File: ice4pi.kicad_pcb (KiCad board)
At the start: 4 copper layers, 85 x 56 mm, 40 parts, among them J1 Conn_02x03, J2 Raspberry_Pi_2_3, J3 USB_C_Receptacle_USB2.0, J4 RJ45_Abracon_ARJP11A-MASA-B-A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, U1 ENC28J60x-SS, U2 DSC1001DE1-025.0000, U3 TPS2375-1

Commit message: fix: better paths
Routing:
- net POE_V-: track 73.7 -> 71.0 mm
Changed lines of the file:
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@@
 	)
 	(via
-		(at 98.5 76.5)
+		(at 101 79)
 		(size 0.8)
 		(drill 0.4)
@@
 	)
 	(segment
-		(start 97 84)
-		(end 97 78)
+		(start 105.5 83.5)
+		(end 105.5 90)
 		(width 1)
 		(layer "In1.Cu")
@@
 	)
 	(segment
-		(start 97 78)
-		(end 98.5 76.5)
-		(width 1)
-		(layer "In1.Cu")
-		(net 50)
-	)
-	(segment
-		(start 105.5 90)
-		(end 103 90)
-		(width 1)
-		(layer "In1.Cu")
-		(net 50)
-	)
-	(segment
-		(start 103 90)
-		(end 97 84)
+		(start 101 79)
+		(end 105.5 83.5)
 		(width 1)
 		(layer "In1.Cu")
@@
 	)
 	(segment
+		(start 101 79)
+		(end 97.4 75.4)
+		(width 1)
+		(layer "B.Cu")
+		(net 50)
+	)
+	(segment
 		(start 107.5 97.5)
 		(end 106 97.5)
@@
 	)
 	(segment
-		(start 98.5 76.5)
-		(end 97.4 75.4)
+		(start 97.4 73.1)
+		(end 102.5 68)
 		(width 1)
 		(layer "B.Cu")
@@
 		(width 1)
 		(layer "B.Cu")
-		(net 50)
-	)
-	(segment
-		(start 97.4 73.1)
-		(end 102.5 68)
-		(width 1)
-		(layer "B.Cu")

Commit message: fix: led
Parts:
- added R12: 332K, Resistor_SMD:R_0402_1005Metric, F.Cu at (103.0, 101.2)
- moved R7 0.10 mm to (132.8, 71.5)
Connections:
- R6 pad 1: /LEDB -> /LEDA
- R6 pad 2: Net-(J4-Pad13) -> Net-(J4-Pad11)
- R7 pad 1: /LEDA -> /LEDB
- R7 pad 2: Net-(J4-Pad11) -> Net-(J4-Pad13)
- U3 pad 6: Net-(LSI-U1-S2) -> Net-(U3-PG)
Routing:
- net (no net): track 23.1 -> 0.00 mm
- net Net-(J4-Pad13): track 0.00 -> 17.3 mm
- net Net-(J4-Pad11): track 0.00 -> 5.77 mm
- net Net-(LSI-U1-S2): track 13.4 -> 11.6 mm
- net Net-(U3-PG): track 0.00 -> 1.62 mm
- net +5V: vias 3 -> 5

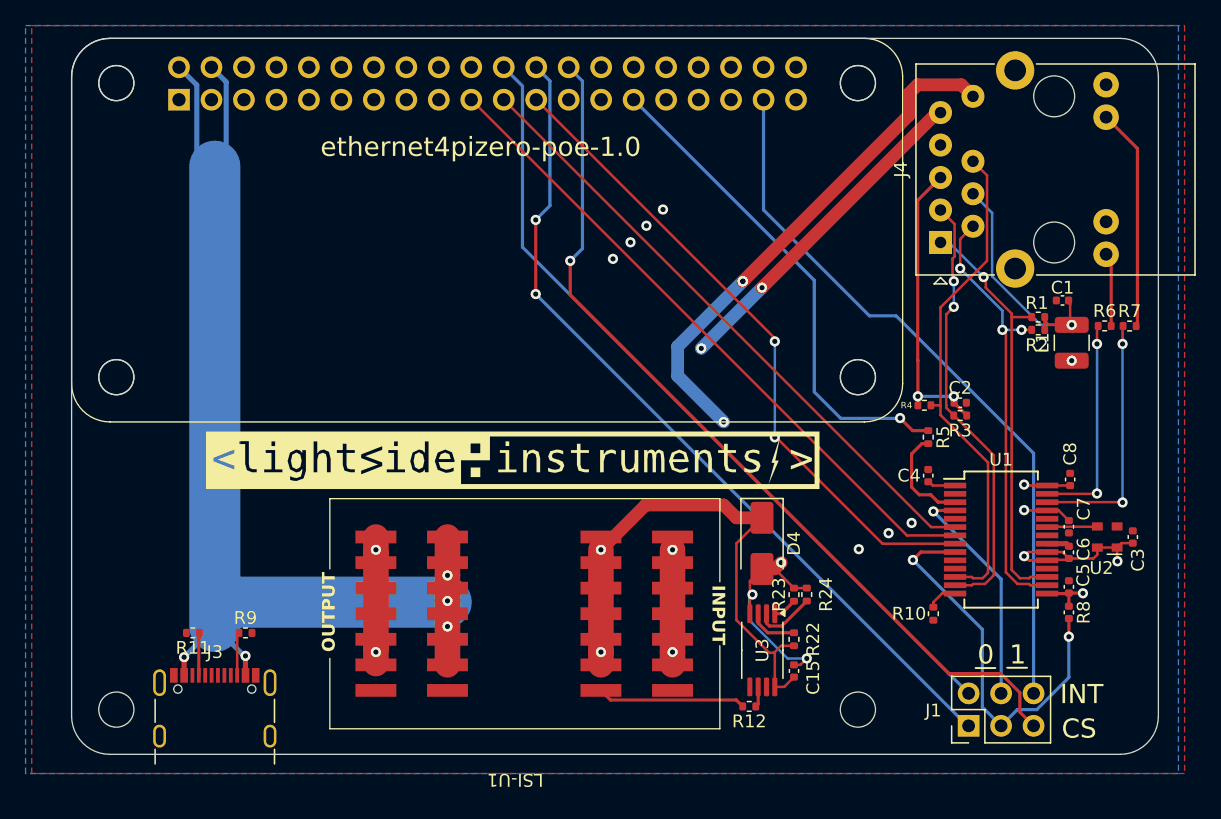
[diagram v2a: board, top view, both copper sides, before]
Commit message: feat: changed power traces layer
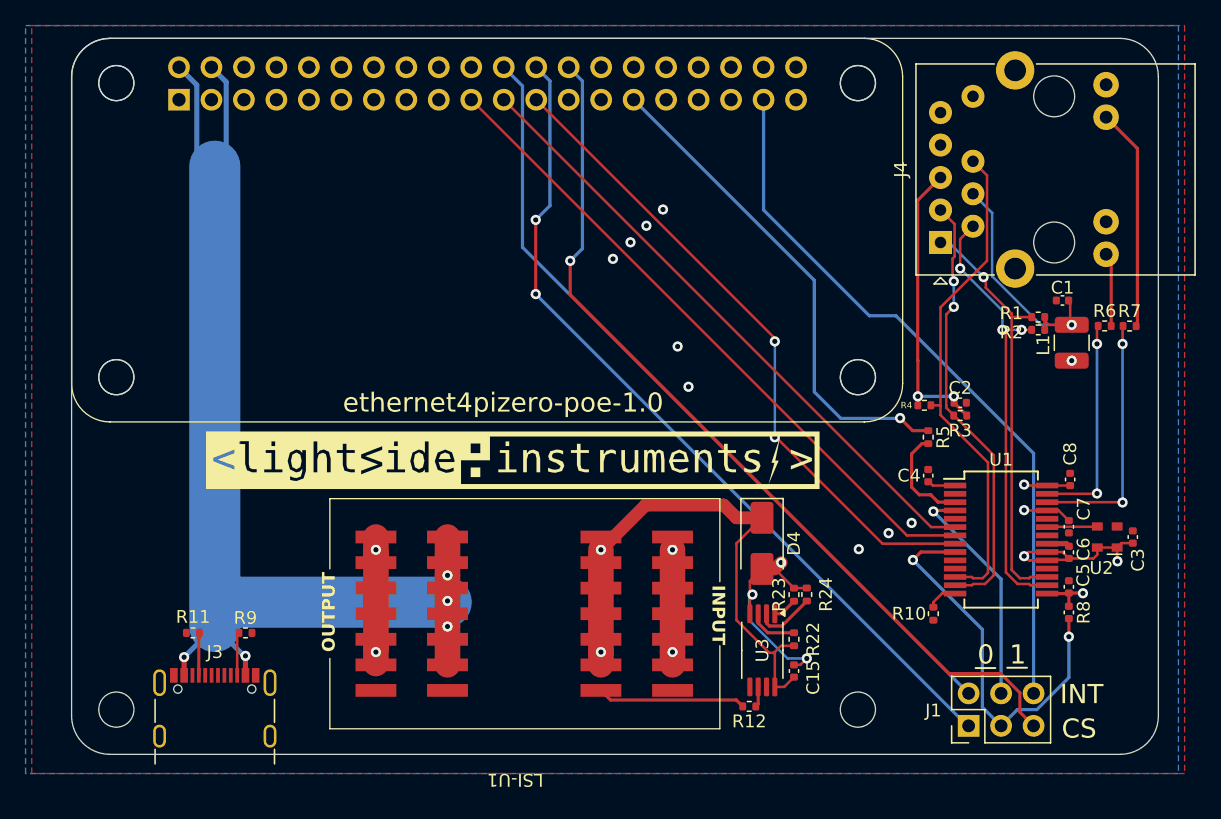
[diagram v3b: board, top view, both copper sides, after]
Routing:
- net POE_V-: track 71.0 -> 69.8 mm, vias 6 -> 5
- net POE_V+: track 96.0 -> 96.3 mm, vias 4 -> 2
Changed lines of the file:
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@@
 		(tags "resistor")
 		(property "Reference" "R2"
-			(at 0.1 -1.2 0)
+			(at 2.1 -0.2 0)
 			(layer "F.SilkS")
 			(effects
@@
 		(tags "resistor")
 		(property "Reference" "R11"
-			(at 0 -1.17 0)
+			(at -0.01 1.25 0)
 			(layer "F.SilkS")
 			(effects
@@
 		(tags "resistor")
 		(property "Reference" "R1"
-			(at 0.1 1.1 0)
+			(at 2.1 0.3 0)
 			(layer "F.SilkS")
 			(effects
@@
 		(tags "inductor")
 		(property "Reference" "L1"
-			(at 0 -2.28 90)
+			(at -0.192889 -2.221383 90)
 			(layer "F.SilkS")
 			(effects
@@
 	)
 	(gr_text "ethernet4pizero-poe-1.0"
-		(at 82 57.5 0)
+		(at 83.75 77.5 0)
 		(layer "F.SilkS")
 		(effects
@@
 	)
 	(segment
-		(start 104 68.5)
-		(end 117.695 54.805)
-		(width 1)
-		(layer "F.Cu")
-		(net 49)
-	)
-	(segment
 		(start 102 86.5)
 		(end 104 86.5)
@@
 		(net 49)
 	)
-	(via
-		(at 99.25 73.25)
-		(size 0.8)
-		(drill 0.4)
-		(layers "F.Cu" "B.Cu")
-		(net 49)
-	)
-	(via
-		(at 104 68.5)
-		(size 0.8)
-		(drill 0.4)
-		(layers "F.Cu" "B.Cu")
-		(net 49)
-	)
-	(segment
-		(start 91.4 81)
-		(end 91.4 89)
-		(width 1)
-		(layer "In1.Cu")
-		(net 49)
-	)
 	(segment
 		(start 91.4 89)
@@
 	)
 	(segment
-		(start 99.25 73.25)
-		(end 99.15 73.25)
+		(start 117.96 54.805)
+		(end 117.595 54.805)
 		(width 1)
 		(layer "In1.Cu")
@@
 	)
 	(segment
-		(start 99.15 73.25)
-		(end 91.4 81)
+		(start 91.4 81)
+		(end 91.4 89)
 		(width 1)
 		(layer "In1.Cu")
@@
 	)
 	(segment
-		(start 99.25 73.25)
-		(end 104 68.5)
+		(start 117.595 54.805)
+		(end 91.4 81)
 		(width 1)
-		(layer "B.Cu")
+		(layer "In1.Cu")
 		(net 49)
 	)
@@
 	)
 	(segment
-		(start 119.6 52.635)
-		(end 120.5 53.535)
-		(width 1)
-		(layer "F.Cu")
-		(net 50)
-	)
-	(segment
 		(start 105 90.5)
 		(end 106.5 92)
@@
 	)
 	(segment
-		(start 115.5 55)
-		(end 102.5 68)
-		(width 1)
-		(layer "F.Cu")
-		(net 50)
-	)
-	(segment
 		(start 104 90.5)
 		(end 105 90.5)
@@
 	)
 	(segment
-		(start 116.17 52.635)
-		(end 119.6 52.635)
-		(width 1)
-		(layer "F.Cu")
-		(net 50)
-	)
-	(segment
-		(start 115.5 53.305)
-		(end 115.5 55)
-		(width 1)
-		(layer "F.Cu")
-		(net 50)
-	)
-	(segment
-		(start 115.5 53.305)
-		(end 116.17 52.635)
-		(width 1)
-		(layer "F.Cu")
-		(net 50)
-	)
-	(segment
 		(start 107.5 97.5)
 		(end 107 98)
@@
 	)
 	(via
-		(at 102.5 68)
-		(size 0.8)
-		(drill 0.4)
-		(layers "F.Cu" "B.Cu")
-		(net 50)
-	)
-	(via
 		(at 103.25 92.5)
 		(size 0.8)
@@
 	)
 	(via
-		(at 101 79)
+		(at 98.25 76.25)
 		(size 0.8)
 		(drill 0.4)
@@
 	)
 	(via
-		(at 102.5 68)
+		(at 97.4 73.1)
 		(size 0.8)
 		(drill 0.4)
@@
 	)
 	(segment
-		(start 101 79)
-		(end 105.5 83.5)
+		(start 116.845 53.155)
+		(end 97.4 72.6)
 		(width 1)
 		(layer "In1.Cu")
@@
 	)
 	(segment
-		(start 103 92.75)
-		(end 103.25 92.5)
-		(width 0.2)
-		(layer "B.Cu")
+		(start 97.4 72.6)
+		(end 97.4 73.1)
+		(width 1)
+		(layer "In1.Cu")
 		(net 50)
 	)
 	(segment
-		(start 106 97.5)
-		(end 103 94.5)
-		(width 0.2)
-		(layer "B.Cu")
+		(start 120.5 53.535)
+		(end 120.12 53.155)
+		(width 1)
+		(layer "In1.Cu")
+		(net 50)
+	)
+	(segment
+		(start 120.12 53.155)
+		(end 116.845 53.155)
+		(width 1)
+		(layer "In1.Cu")
+		(net 50)
+	)
+	(segment
+		(start 98.25 76.25)
+		(end 105.5 83.5)
+		(width 1)
+		(layer "In1.Cu")
+		(net 50)
+	)
+	(segment
+		(start 97.4 75.4)
+		(end 98.25 76.25)
+		(width 1)
+		(layer "In2.Cu")
 		(net 50)
 	)
 	(segment
-		(start 101 79)
+		(start 97.4 73.1)
 		(end 97.4 75.4)
 		(width 1)
-		(layer "B.Cu")
+		(layer "In2.Cu")
 		(net 50)
 	)
 	(segment
-		(start 107.5 97.5)
-		(end 106 97.5)
+		(start 103 92.75)
+		(end 103.25 92.5)
 		(width 0.2)
 		(layer "B.Cu")
@@
 	)
 	(segment
-		(start 97.4 73.1)
-		(end 102.5 68)
-		(width 1)
+		(start 106 97.5)
+		(end 103 94.5)
+		(width 0.2)
 		(layer "B.Cu")
 		(net 50)
 	)
 	(segment
-		(start 97.4 75.4)
-		(end 97.4 73.1)
-		(width 1)
+		(start 107.5 97.5)
+		(end 106 97.5)
+		(width 0.2)
 		(layer "B.Cu")
 		(net 50)

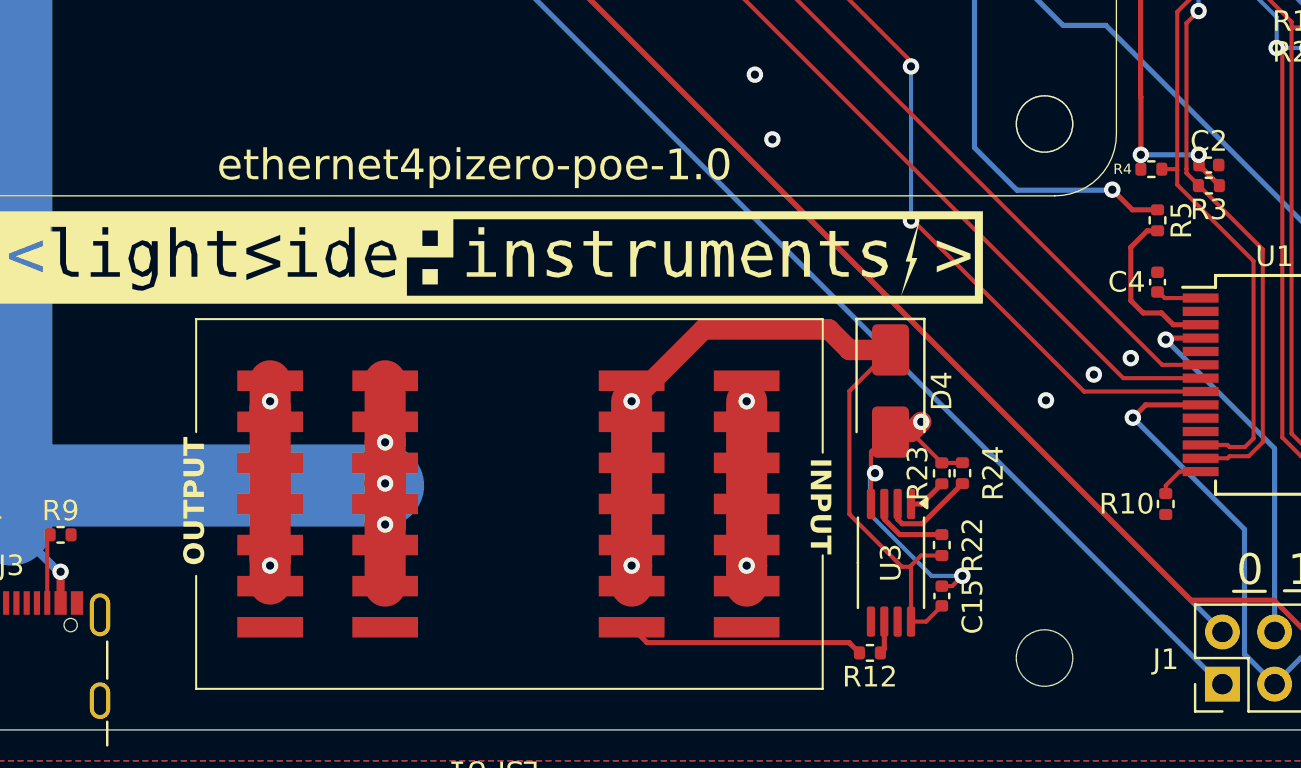
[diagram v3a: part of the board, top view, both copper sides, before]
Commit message: fix: using correct powermod footprint
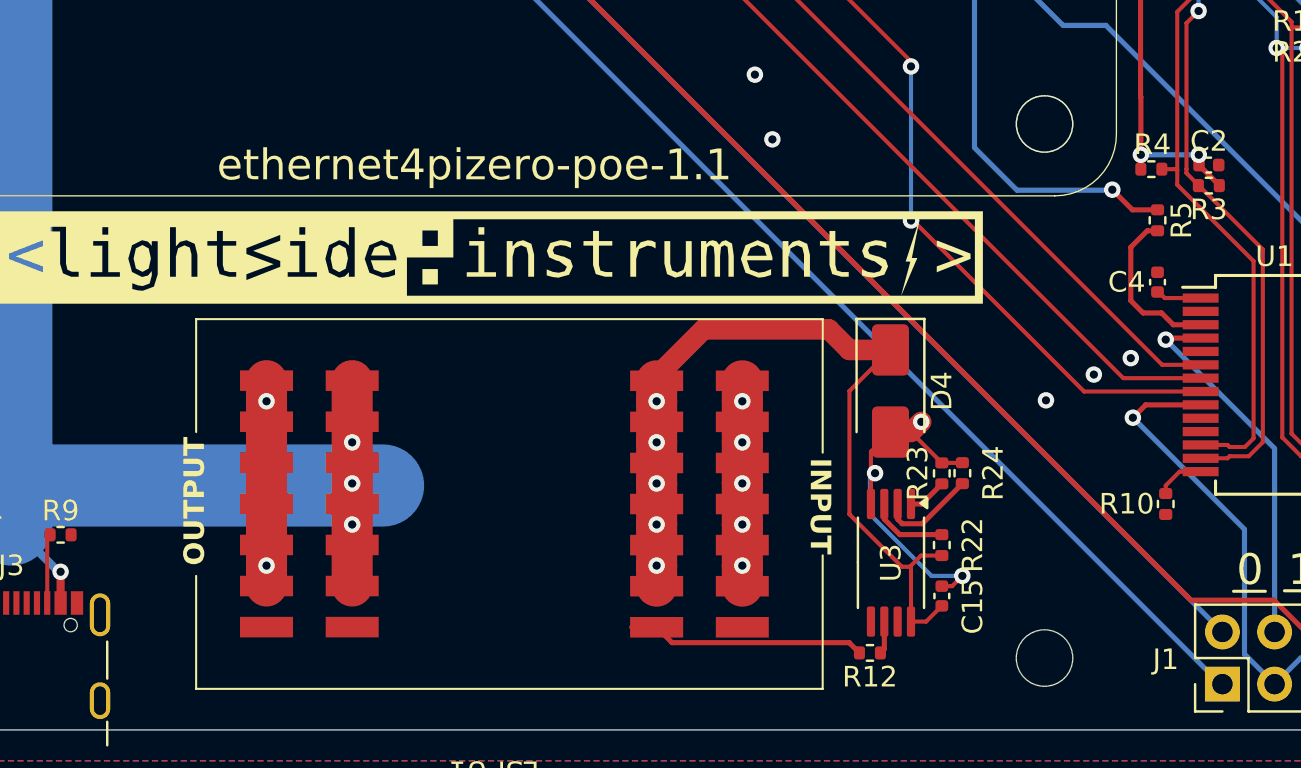
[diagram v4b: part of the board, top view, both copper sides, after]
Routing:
- net +5V: track 94.2 -> 95.6 mm
- net POE_V+: track 96.3 -> 96.7 mm, vias 2 -> 5
- net GND: track 23.6 -> 23.3 mm, vias 11 -> 14
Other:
- board text added: "ethernet4pizero-poe-1.1"
- board text removed: "ethernet4pizero-poe-1.0"

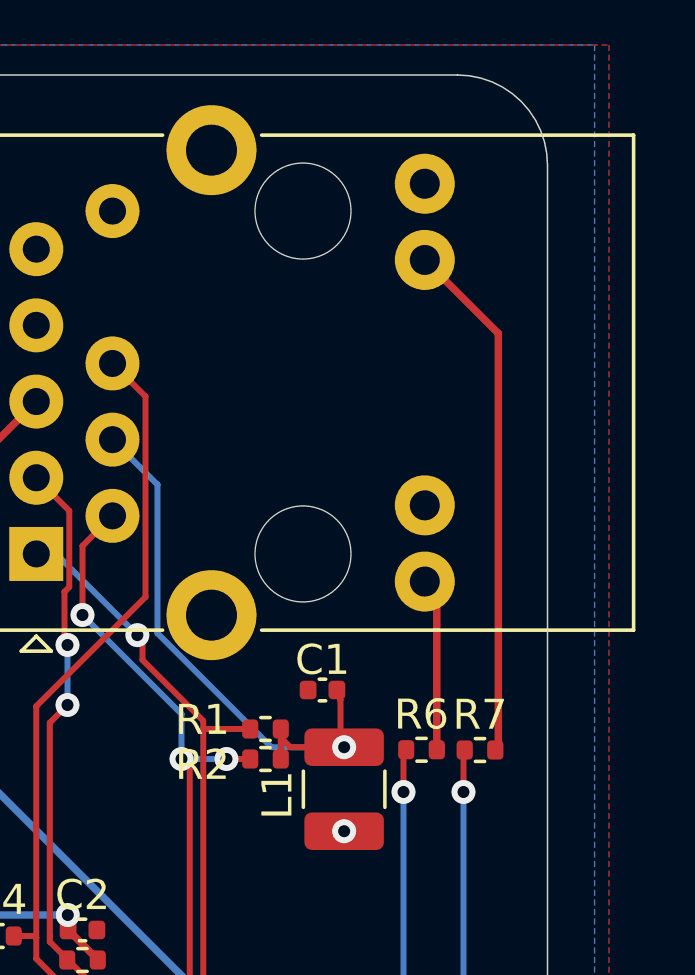
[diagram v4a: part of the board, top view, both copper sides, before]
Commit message: fix: fixed led polarity
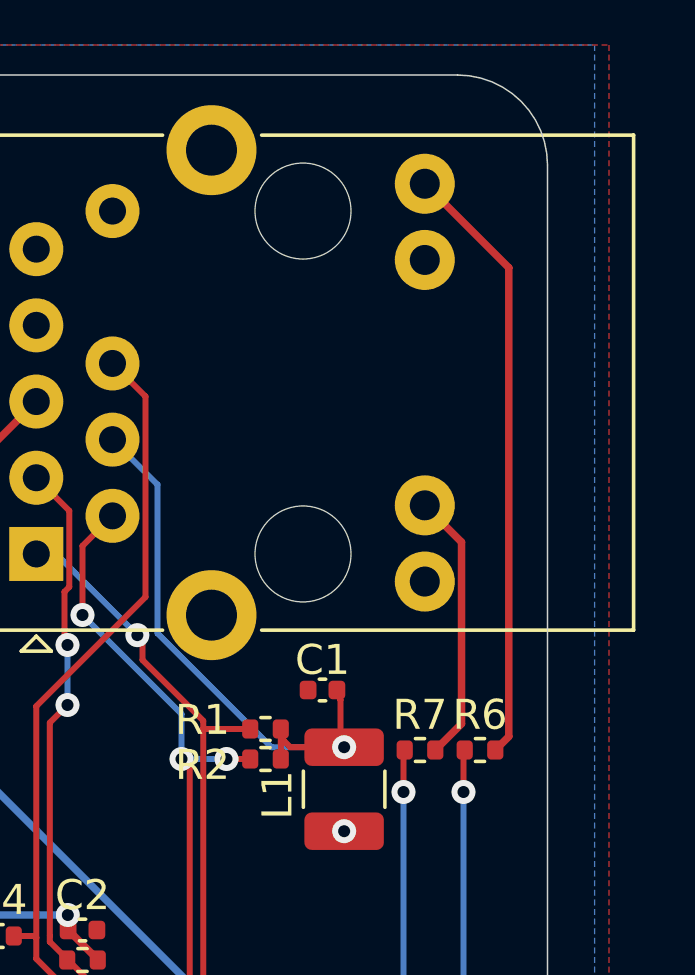
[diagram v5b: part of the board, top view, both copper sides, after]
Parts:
- moved R7 2.00 mm to (130.8, 71.5)
- moved R6 1.95 mm to (132.8, 71.5)
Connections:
- J4 pad 11: Net-(J4-Pad11) -> GND
- J4 pad 12: GND -> Net-(J4-Pad12)
- J4 pad 13: Net-(J4-Pad13) -> GND
- J4 pad 14: GND -> Net-(J4-Pad14)
- R6 pad 1: /LEDA -> /LEDB
- R6 pad 2: Net-(J4-Pad11) -> Net-(J4-Pad14)
- R7 pad 1: /LEDB -> /LEDA
- R7 pad 2: Net-(J4-Pad13) -> Net-(J4-Pad12)
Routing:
- net Net-(J4-Pad14): track 0.00 -> 21.6 mm
- net Net-(J4-Pad13): track 17.3 -> 0.00 mm
- net Net-(J4-Pad12): track 0.00 -> 9.02 mm
- net Net-(J4-Pad11): track 5.77 -> 0.00 mm
- net GND: track 23.3 -> 22.5 mm
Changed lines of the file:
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@@
 	(net 65 "Net-(J4-TCT)")
 	(net 66 "Net-(J4-RCT)")
-	(net 67 "Net-(J4-Pad11)")
-	(net 68 "Net-(J4-Pad13)")
-	(net 69 "unconnected-(J4-Pad7)")
-	(net 70 "Net-(U3-PG)")
+	(net 67 "unconnected-(J4-Pad7)")
+	(net 68 "Net-(U3-PG)")
+	(net 69 "Net-(J4-Pad14)")
+	(net 70 "Net-(J4-Pad12)")
 	(footprint "ice4pi:mount_hole"
 		(locked yes)
@@
 	(footprint "Resistor_SMD:R_0402_1005Metric"
 		(layer "F.Cu")
-		(at 130.800732 71.491962)
+		(at 132.75 71.5)
 		(descr "Resistor SMD 0402 (1005 Metric), square (rectangular) end terminal, IPC_7351 nominal, (Body size source: IPC-SM-782 page 72, https://www.pcb-3d.com/wordpress/wp-content/uploads/ipc-sm-782a_amendment_1_and_2.pdf), generated with kicad-footprint-generator")
 		(tags "resistor")
@@
 			(layers "F.Cu" "F.Paste" "F.Mask")
 			(roundrect_rratio 0.25)
-			(net 43 "/LEDA")
+			(net 42 "/LEDB")
 			(pintype "passive")
 		)
@@
 			(layers "F.Cu" "F.Paste" "F.Mask")
 			(roundrect_rratio 0.25)
-			(net 67 "Net-(J4-Pad11)")
+			(net 69 "Net-(J4-Pad14)")
 			(pintype "passive")
 		)
@@
 	(footprint "Resistor_SMD:R_0402_1005Metric"
 		(layer "F.Cu")
-		(at 132.75 71.5)
+		(at 130.75 71.5)
 		(descr "Resistor SMD 0402 (1005 Metric), square (rectangular) end terminal, IPC_7351 nominal, (Body size source: IPC-SM-782 page 72, https://www.pcb-3d.com/wordpress/wp-content/uploads/ipc-sm-782a_amendment_1_and_2.pdf), generated with kicad-footprint-generator")
 		(tags "resistor")
@@
 			(layers "F.Cu" "F.Paste" "F.Mask")
 			(roundrect_rratio 0.25)
-			(net 42 "/LEDB")
+			(net 43 "/LEDA")
 			(pintype "passive")
 		)
@@
 			(layers "F.Cu" "F.Paste" "F.Mask")
 			(roundrect_rratio 0.25)
-			(net 68 "Net-(J4-Pad13)")
+			(net 70 "Net-(J4-Pad12)")
 			(pintype "passive")
 		)
@@
 			(layers "*.Cu" "*.Mask")
 			(remove_unused_layers no)
-			(net 69 "unconnected-(J4-Pad7)")
+			(net 67 "unconnected-(J4-Pad7)")
 			(pintype "power_in+no_connect")
 		)
@@
 			(layers "*.Cu" "*.Mask")
 			(remove_unused_layers no)
-			(net 67 "Net-(J4-Pad11)")
+			(net 1 "GND")
 			(pintype "passive")
 		)
@@
 			(layers "*.Cu" "*.Mask")
 			(remove_unused_layers no)
-			(net 1 "GND")
+			(net 70 "Net-(J4-Pad12)")
 			(pintype "passive")
 		)
@@
 			(layers "*.Cu" "*.Mask")
 			(remove_unused_layers no)
-			(net 68 "Net-(J4-Pad13)")
+			(net 1 "GND")
 			(pintype "passive")
 		)
@@
 			(layers "*.Cu" "*.Mask")
 			(remove_unused_layers no)
-			(net 1 "GND")
+			(net 69 "Net-(J4-Pad14)")
 			(pintype "passive")
 		)
@@
 			(layers "F.Cu" "F.Paste" "F.Mask")
 			(roundrect_rratio 0.25)
-			(net 70 "Net-(U3-PG)")
+			(net 68 "Net-(U3-PG)")
 			(pinfunction "PG")
 			(pintype "open_collector")
@@
 			(layers "F.Cu" "F.Paste" "F.Mask")
 			(roundrect_rratio 0.25)
-			(net 70 "Net-(U3-PG)")
+			(net 68 "Net-(U3-PG)")
 			(pintype "passive")
 		)
@@
 	)
 	(segment
+		(start 131.310732 66.285732)
+		(end 130.91 65.885)
+		(width 0.25)
+		(layer "F.Cu")
+		(net 1)
+	)
+	(segment
 		(start 73.625015 87.994762)
 		(end 73.625015 89)
@@
 	)
 	(segment
-		(start 131.556431 52.925)
-		(end 130.22 52.925)
-		(width 0.2)
-		(layer "F.Cu")
-		(net 1)
-	)
-	(segment
 		(start 96.787024 98.001469)
 		(end 96.787024 97)
@@
 	)
 	(segment
-		(start 132.2 72.9)
-		(end 132.2 71.41)
+		(start 132.2 71.54)
+		(end 132.24 71.5)
 		(width 0.2)
 		(layer "F.Cu")
@@
 		(net 42)
 	)
+	(segment
+		(start 132.2 72.9)
+		(end 132.2 71.54)
+		(width 0.2)
+		(layer "F.Cu")
+		(net 42)
+	)
 	(via
 		(at 132.2 85.3)
@@
 	(segment
 		(start 130.2 72.9)
-		(end 130.2 71.41)
+		(end 130.2 71.54)
 		(width 0.2)
 		(layer "F.Cu")
@@
 	)
 	(segment
+		(start 130.2 71.54)
+		(end 130.24 71.5)
+		(width 0.2)
+		(layer "F.Cu")
+		(net 43)
+	)
+	(segment
 		(start 130.175 84.625)
 		(end 130.2 84.6)
@@
 	)
 	(segment
-		(start 131.310732 66.285732)
-		(end 130.91 65.885)
+		(start 103.5 101.26)
+		(end 103.7 101.06)
 		(width 0.25)
 		(layer "F.Cu")
-		(net 67)
+		(net 68)
 	)
 	(segment
-		(start 131.310732 71.491962)
-		(end 131.310732 66.285732)
+		(start 103.7 101.06)
+		(end 103.7 99.725)
 		(width 0.25)
 		(layer "F.Cu")
-		(net 67)
+		(net 68)
 	)
 	(segment
-		(start 133.359536 57.614536)
-		(end 130.91 55.165)
+		(start 133.709536 71.050464)
+		(end 133.709536 55.424536)
 		(width 0.25)
 		(layer "F.Cu")
-		(net 68)
+		(net 69)
 	)
 	(segment
-		(start 133.359536 71.499999)
-		(end 133.359536 57.614536)
+		(start 133.709536 55.424536)
+		(end 130.91 52.625)
 		(width 0.25)
 		(layer "F.Cu")
-		(net 68)
+		(net 69)
 	)
 	(segment
-		(start 103.5 101.26)
-		(end 103.7 101.06)
+		(start 131.556431 52.925)
+		(end 130.22 52.925)
+		(width 0.2)
+		(layer "F.Cu")
+		(net 69)
+	)
+	(segment
+		(start 133.26 71.5)
+		(end 133.709536 71.050464)
+		(width 0.25)
+		(layer "F.Cu")
+		(net 69)
+	)
+	(segment
+		(start 132.135 70.625)
+		(end 132.135 64.57)
 		(width 0.25)
 		(layer "F.Cu")
@@
 	)
 	(segment
-		(start 103.7 101.06)
-		(end 103.7 99.725)
+		(start 132.135 64.57)
+		(end 130.91 63.345)
+		(width 0.25)
+		(layer "F.Cu")
+		(net 70)
+	)
+	(segment
+		(start 131.26 71.5)
+		(end 132.135 70.625)
 		(width 0.25)
 		(layer "F.Cu")
